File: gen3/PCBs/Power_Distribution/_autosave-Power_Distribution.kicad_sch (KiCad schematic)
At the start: 62 parts, among them IC1 ACS713ELCTR-30A-T, IC2 ACS713ELCTR-30A-T, IC3 ACS713ELCTR-30A-T, IC4 ACS713ELCTR-30A-T, IC5 ACS713ELCTR-30A-T, IC6 ACS713ELCTR-30A-T, IC7 ACS713ELCTR-30A-T, IC8 ACS713ELCTR-30A-T, J1 1098169, J10 430450228, J11 430450228, J12 430450228, J13 430450228, J14 430450228, J15 430450228, J16 430450228, J17 430450228, J18 SBH11-PBPC-D10-ST-BK, J2 1098169, J3 Conn_01x08, J4 Conn_01x02_Pin, J5 Conn_01x02_Pin, J6 1098169, J7 1098169, J9 Conn_01x08, U1 MCP9808_MSOP, U2 MCP9808_MSOP

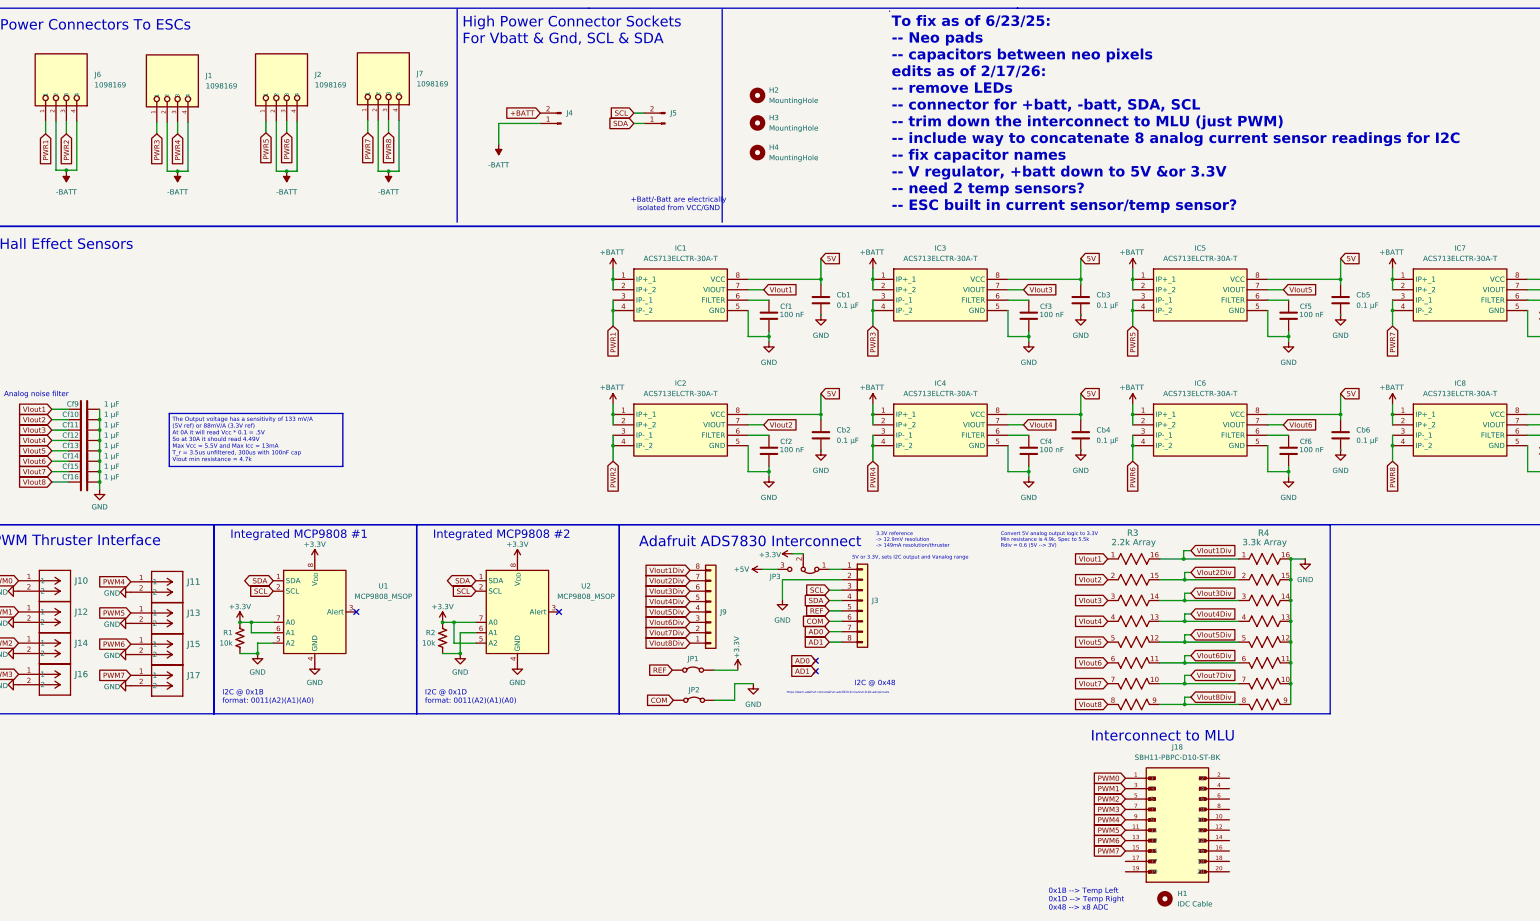
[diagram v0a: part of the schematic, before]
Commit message: power dist fixes 1
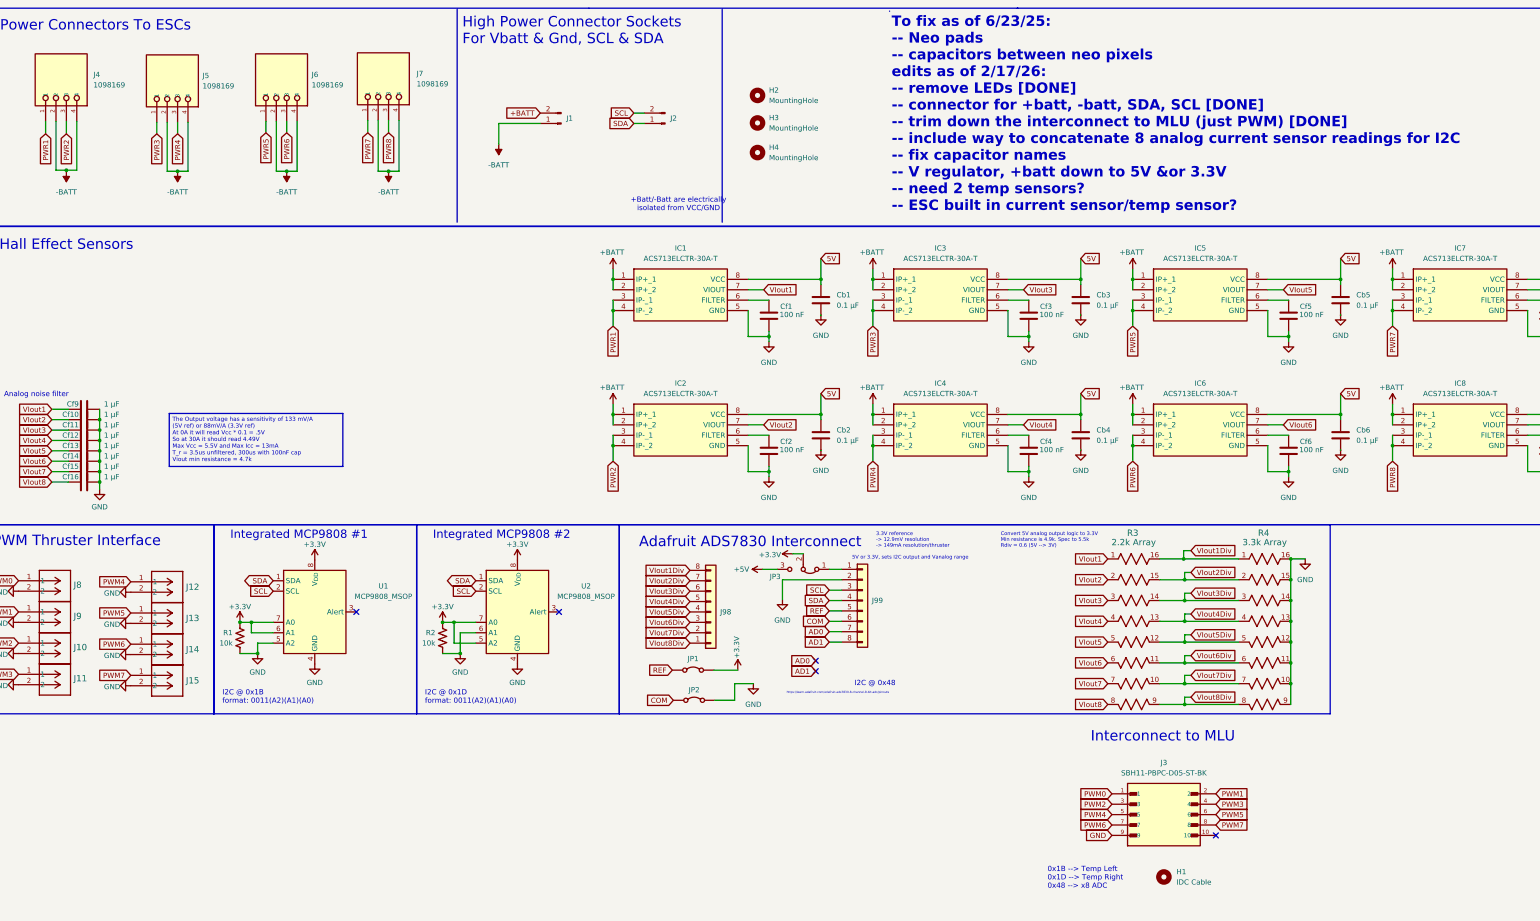
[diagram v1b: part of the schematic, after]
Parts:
- removed J18: SBH11-PBPC-D10-ST-BK, Imported_Footprints:SULLINS_SBH11-PBPC-D10-ST-BK, symbol Imported_Symbols:SBH11-PBPC-D10-ST-BK
- added J3: SBH11-PBPC-D05-ST-BK, Imported_Footprints:SULLINS_SBH11-PBPC-D05-ST-BK, symbol Imported_Symbols:SBH11-PBPC-D05-ST-BK
- renumbered J4 to J1, J14 to J10, J16 to J11, J11 to J12, J15 to J14, J17 to J15, J5 to J2, J6 to J4, J1 to J5, J2 to J6, J10 to J8, J12 to J9, J9 to J98, J3 to J99
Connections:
- net GND: now also J3.9
- net PWM0: now also J3.1
- net PWM1: now also J3.2
- net PWM2: now also J3.3
- net PWM3: now also J3.4
- net PWM4: now also J3.5
- net PWM5: now also J3.6
- net PWM6: now also J3.7
- net PWM7: now also J3.8
- no-connect marks 4 -> 5
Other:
- note added: "To fix as of 6/23/25: -- Neo pads -- capacitors between neo pixels edits as of 2/17/26: -- remove LEDs [DONE] -- connector for +batt, -batt, SDA, SCL [DONE] -- trim down the interconnect to MLU (just PWM) [DONE] -- include way to concatenate 8 analog current sensor readings for I2C -- fix capacitor names -- V regulator, +batt down to 5V &or 3.3V -- need 2 temp sensors? -- ESC built in current sen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"
- note removed: "To fix as of 6/23/25: -- Neo pads -- capacitors between neo pixels edits as of 2/17/26: -- remove LEDs -- connector for +batt, -batt, SDA, SCL -- trim down the interconnect to MLU (just PWM) -- include way to concatenate 8 analog current sensor readings for I2C -- fix capacitor names -- V regulator, +batt down to 5V &or 3.3V -- need 2 temp sensors? -- ESC built in current sensor/temp sensor?"
- title: Test sheet -> Power distribution board
- moved on the sheet: H1
